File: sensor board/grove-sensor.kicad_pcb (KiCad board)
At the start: 2 copper layers, 71.8 x 71.8 mm, 27 parts, among them P1 CONN_01X03, P2 CONN_01X03, P3 CONN_01X03, P4 CONN_01X04, Q1 PN2222A, U2 SI1143, U3 Teensy_3.1

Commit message: bunch of sensor stuff
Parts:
- added P10: CONN_01X01, Pin_Headers:Pin_Header_Straight_1x01, F.Cu at (174.0, 94.0)
- added P11: CONN_01X01, Pin_Headers:Pin_Header_Straight_1x01, F.Cu at (173.5, 97.8)
- added P12: CONN_01X01, Pin_Headers:Pin_Header_Straight_1x01, F.Cu at (172.3, 101.6)
- added P13: CONN_01X01, Pin_Headers:Pin_Header_Straight_1x01, F.Cu at (170.6, 105.4)
- added P5: CONN_01X01, Pin_Headers:Pin_Header_Straight_1x01, F.Cu at (123.7, 87.8)
- added P6: CONN_01X01, Pin_Headers:Pin_Header_Straight_1x01, F.Cu at (123.2, 91.4)
- added P7: CONN_01X01, Pin_Headers:Pin_Header_Straight_1x01, F.Cu at (171.8, 82.5)
- added P8: CONN_01X01, Pin_Headers:Pin_Header_Straight_1x01, F.Cu at (173.2, 86.4)
- added P9: CONN_01X01, Pin_Headers:Pin_Header_Straight_1x01, F.Cu at (173.9, 90.2)
- added U1: ADD8704, SI1143:TSSOP-14, F.Cu at (163.8, 104.1)
- D1, D2, D3: footprint LEDs:LED-5MM -> LEDs:LED_0805
- P1, P2, P3: value CONN_01X03 -> CONN_01X01; footprint Pin_Headers:Pin_Header_Straight_1x03 -> Pin_Headers:Pin_Header_Straight_1x01
- P4: value CONN_01X04 -> CONN_01X01; footprint Pin_Headers:Pin_Header_Straight_1x04 -> Pin_Headers:Pin_Header_Straight_1x01
- Q1: footprint TO_SOT_Packages_THT:TO-92_Horizontal1_Inline_Narrow_Oval -> TO_SOT_Packages_SMD:SOT-23_Handsoldering
- moved R5 73.9 mm to (151.1, 102.9), turned to 90 degrees
- moved R2 67.3 mm to (144.8, 102.9), turned to 90 degrees
- moved R10 44.5 mm to (165.1, 133.3)
- moved R11 44.5 mm to (148.6, 133.3)
- moved R6 44.5 mm to (152.4, 135.9)
- moved R7 44.5 mm to (143.5, 135.9)
- moved R9 44.5 mm to (160.0, 135.9)
- moved R13 44.5 mm to (139.7, 121.9)
- moved R3 44.5 mm to (157.5, 124.5)
- moved C1 44.5 mm to (152.4, 123.2)
- moved C2 44.5 mm to (143.5, 130.8)
- moved C3 44.5 mm to (148.6, 123.2)
- moved R12 44.5 mm to (138.4, 128.3)
- moved R14 44.5 mm to (152.4, 128.9)
- moved R4 44.5 mm to (161.3, 128.3)
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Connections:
- P1 pad 1: GND -> +5V
- P2 pad 1: GND -> +5V
- P3 pad 1: GND -> /RGB2
- U3 pad 24: Net-(U3-Pad24) -> /3.3V
- U3 pad 3: Net-(P3-Pad2) -> Net-(P8-Pad1)
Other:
- board size 71.8 x 71.8 mm -> 50.8 x 50.8 mm

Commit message: Some fixes and placement changes
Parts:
- removed P2, P3, P4, P5, P6: CONN_01X01, Pin_Headers:Pin_Header_Straight_1x01
- added D4: LED_RGB, LEDs:LED_WS2812-PLCC6, F.Cu at (162.6, 84.3)
- added D5: LED_RGB, LEDs:LED_WS2812-PLCC6, F.Cu at (132.1, 84.6)
- added R15: 100, Resistors_SMD:R_0603_HandSoldering, F.Cu at (155.2, 86.4)
- added R16: 100, Resistors_SMD:R_0603_HandSoldering, F.Cu at (155.2, 84.3)
- added R17: 100, Resistors_SMD:R_0603_HandSoldering, F.Cu at (155.2, 82.3)
- added R18: 100, Resistors_SMD:R_0603_HandSoldering, F.Cu at (139.3, 82.4)
- added R19: 100, Resistors_SMD:R_0603_HandSoldering, F.Cu at (139.3, 84.5)
- added R20: 100, Resistors_SMD:R_0603_HandSoldering, F.Cu at (139.3, 86.5)
- moved R9 53.6 mm to (125.0, 95.4), turned to 270 degrees
- moved R10 50.8 mm to (126.4, 100.5), turned to 270 degrees
- moved R11 48.5 mm to (125.1, 90.9), turned to 90 degrees
- moved P1 45.3 mm to (169.9, 79.0)
- moved C2 41.8 mm to (128.4, 91.8)
- moved R8 40.2 mm to (135.0, 100.6), turned to 90 degrees
- moved R7 40.1 mm to (139.1, 96.0), turned to 270 degrees
- moved R6 37.5 mm to (139.1, 100.8), turned to 90 degrees
- moved R4 34.3 mm to (134.7, 106.6), turned to 180 degrees
- moved U1 32.7 mm to (132.2, 95.9), turned to 90 degrees
- moved C1 31.1 mm to (137.3, 96.0), turned to 270 degrees
- moved C3 29.1 mm to (153.9, 94.6), turned to 180 degrees
- moved R12 28.4 mm to (129.0, 101.5), turned to 90 degrees
- moved R3 28.4 mm to (137.5, 104.3), turned to 180 degrees
- moved R13 18.4 mm to (130.2, 106.2), turned to 180 degrees
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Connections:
- net /PROX_INT renamed Net-(U2-Pad4)
- C2 pad 1: /OUT -> Net-(C2-Pad1)
- P1 pad 1: +5V -> /PIR_IN
- R12 pad 1: Net-(R12-Pad1) -> Net-(C2-Pad1)
- R13 pad 2: /OUT -> Net-(C2-Pad1)
- R7 pad 2: Net-(R7-Pad2) -> Net-(R5-Pad1)
- U1 pad 8: Net-(R12-Pad1) -> Net-(C2-Pad1)
- U3 pad 20: Net-(U3-Pad20) -> /PIR_IN
- U3 pad 4: Net-(U3-Pad4) -> /LED1_R
- U3 pad 5: Net-(U3-Pad5) -> /LED1_G
- U3 pad 6: Net-(U3-Pad6) -> /LED1_B
- U3 pad 7: Net-(U3-Pad7) -> /LED2_R
- U3 pad 8: Net-(U3-Pad8) -> /LED2_G
- U3 pad 9: Net-(U3-Pad9) -> /LED2_B
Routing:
- net GND: track 0.00 -> 11.3 mm, vias 0 -> 5
- net Net-(C2-Pad2): track 0.00 -> 11.0 mm
- net Net-(R11-Pad1): track 0.00 -> 9.42 mm, vias 0 -> 2
- net /SENSITIVITY: track 0.00 -> 7.81 mm
- net Net-(C2-Pad1): track 0.00 -> 3.97 mm
- net Net-(D5-Pad6): track 0.00 -> 3.87 mm
- net Net-(D5-Pad4): track 0.00 -> 3.77 mm
- net Net-(D5-Pad5): track 0.00 -> 3.69 mm
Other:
- outline, holes or cut-outs redrawn
- copper layers 2 -> 4

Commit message: Draft sensor route on 4 layers
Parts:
- moved U3 31.8 mm to (162.6, 76.2), turned to 180 degrees
- moved D5 31.2 mm to (163.3, 84.2), turned to 180 degrees
- moved D4 28.3 mm to (134.2, 84.1), turned to 0 degrees
- moved D2 25.0 mm to (159.6, 97.0)
- moved D1 20.4 mm to (138.9, 112.3)
- moved D3 20.1 mm to (158.1, 112.3), turned to 270 degrees
- moved R14 18.4 mm to (163.8, 98.0), turned to 180 degrees
- moved U2 18.2 mm to (148.3, 96.1), turned to 90 degrees
- moved R20 17.3 mm to (156.1, 82.3), turned to 0 degrees
- moved R18 17.2 mm to (156.1, 86.4), turned to 0 degrees
- moved C3 16.8 mm to (162.2, 109.2), turned to 90 degrees
- moved R19 16.8 mm to (156.1, 84.3), turned to 0 degrees
- moved R1 15.5 mm to (142.7, 98.4)
- moved R15 14.3 mm to (141.6, 82.0), turned to 180 degrees
- moved R17 14.1 mm to (141.6, 86.1), turned to 180 degrees
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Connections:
- U3 pad 4: /LED1_R -> /LED1_B
- U3 pad 6: /LED1_B -> /LED1_R
- U3 pad 7: /LED2_R -> /LED2_B
- U3 pad 9: /LED2_B -> /LED2_R
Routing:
- net /MISO: track 0.00 -> 55.1 mm
- net /MOSI: track 0.00 -> 51.4 mm
- net Net-(C3-Pad2): track 0.00 -> 44.3 mm
- net /V_RAW: track 0.00 -> 37.1 mm
- net /PIR_IN: track 0.00 -> 34.1 mm, vias 0 -> 2
- net Net-(R5-Pad1): track 0.00 -> 32.4 mm, vias 0 -> 3
- net /3.3V: track 0.00 -> 25.6 mm, vias 0 -> 1
- net Net-(P8-Pad1): track 0.00 -> 25.0 mm
- net Net-(R1-Pad2): track 0.00 -> 24.9 mm, vias 0 -> 2
- net Net-(D3-Pad1): track 0.00 -> 24.0 mm
- net Net-(D1-Pad1): track 0.00 -> 23.1 mm, vias 0 -> 2
- net Net-(C2-Pad1): track 3.97 -> 25.0 mm, vias 0 -> 2
- net Net-(C2-Pad2): track 11.0 -> 30.2 mm, vias 0 -> 2
- net /LED1_R: track 0.00 -> 17.3 mm
- net +5V: track 0.00 -> 13.4 mm, vias 0 -> 7
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- added copper zone on Power, net +5V
- added copper zone on Ground, net GND
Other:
- outline, holes or cut-outs redrawn
- net class Default: clearance 0.2 -> 0.127; trace_width 0.25 -> 0.127; via_dia 0.6 -> 0.4572; via_drill 0.4 -> 0.254
- rule trace_clearance: 0.2 -> 0.127
- rule trace_min: 0.2 -> 0.127
- rule via_min_drill: 0.3 -> 0.254
- rule via_min_size: 0.4 -> 0.4572

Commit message: Fixes and updates to sensor board
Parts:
- removed D4, D5: LED_RGB, LEDs:LED_WS2812-PLCC6
- removed P10, P11, P12, P13: CONN_01X01, Pin_Headers:Pin_Header_Straight_1x01
- removed R15, R16, R17, R18, R19, R20: 100, Resistors_SMD:R_0603_HandSoldering
- added C4: 10uF, Capacitors_SMD:C_0603_HandSoldering, F.Cu at (143.5, 69.6)
- added C5: 0.1uF, Capacitors_SMD:C_0603_HandSoldering, F.Cu at (138.0, 88.9)
- added C6: 0.1uF, Capacitors_SMD:C_0603_HandSoldering, F.Cu at (161.4, 78.7)
- added P2: CONN_01X06, Pin_Headers:Pin_Header_Straight_1x06, F.Cu at (155.1, 72.0)
- added P3: CONN_01X01, Pin_Headers:Pin_Header_Straight_1x01, F.Cu at (171.6, 98.6)
- added P4: CONN_01X01, Pin_Headers:Pin_Header_Straight_1x01, F.Cu at (171.6, 93.0)
- added R21: 0, Resistors_SMD:R_0603_HandSoldering, F.Cu at (142.9, 95.0)
- added R22: 0, Resistors_SMD:R_0603_HandSoldering, F.Cu at (144.7, 95.0)
- added R23: 10k, Resistors_SMD:R_0603_HandSoldering, F.Cu at (154.4, 98.3)
- added R24: 10k, Resistors_SMD:R_0603_HandSoldering, F.Cu at (154.4, 96.9)
- added R25: 0, Resistors_SMD:R_0603_HandSoldering, F.Cu at (132.5, 83.7)
- added R26: 10k, Resistors_SMD:R_0603_HandSoldering, F.Cu at (167.1, 87.8)
- added U4: MCP1700, TO_SOT_Packages_SMD:SOT-23, F.Cu at (166.5, 94.9)
- added U5: WS2812B, LEDs:LED_WS2812B-PLCC4, F.Cu at (138.7, 84.1)
- added U6: WS2812B, LEDs:LED_WS2812B-PLCC4, F.Cu at (161.0, 83.8)
- Q1: value PN2222A -> Q_NPN_BEC; footprint TO_SOT_Packages_SMD:SOT-23_Handsoldering -> TO_SOT_Packages_SMD:SOT-23
- R2: footprint Resistors_SMD:R_0402 -> Resistors_SMD:R_0603
- moved P1 16.8 mm to (171.6, 95.8)
- moved Q1 1.08 mm to (132.7, 102.9), turned to 180 degrees
- moved R1 0.51 mm to (142.7, 98.9)
- moved P9 0.13 mm to (173.7, 89.7)
- moved R5 0.09 mm to (151.5, 106.6)
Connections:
- net /CS renamed Net-(U3-Pad10)
- Q1 pad 1: /V_RAW -> Net-(Q1-Pad1)
- Q1 pad 2: Net-(Q1-Pad2) -> /V_RAW
- R8 pad 1: Net-(Q1-Pad2) -> Net-(Q1-Pad1)
- U2 pad 1: /SDA -> Net-(R21-Pad1)
- U2 pad 2: /SCL -> Net-(R22-Pad1)
- U3 pad 1: /RGB1 -> Net-(P2-Pad2)
- U3 pad 11: /MOSI -> Net-(U3-Pad11)
- U3 pad 12: /MISO -> Net-(U3-Pad12)
- U3 pad 2: /RGB2 -> Net-(P2-Pad4)
- U3 pad 4: /LED1_B -> Net-(U3-Pad4)
- U3 pad 5: /LED1_G -> Net-(U3-Pad5)
- U3 pad 6: /LED1_R -> Net-(U3-Pad6)
- U3 pad 7: /LED2_B -> Net-(U3-Pad7)
- U3 pad 8: /LED2_G -> /LED_IN
- U3 pad 9: /LED2_R -> Net-(U3-Pad9)
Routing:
- net /MISO: track 55.1 -> 0.00 mm
- net /MOSI: track 51.4 -> 0.00 mm
- net Net-(P2-Pad4): track 0.00 -> 42.8 mm
- net +5V: track 13.4 -> 38.6 mm, vias 7 -> 10
- net Net-(U5-Pad2): track 0.00 -> 23.5 mm
- net /LED1_R: track 17.3 -> 0.00 mm
- net Net-(P2-Pad3): track 0.00 -> 16.3 mm
- net Net-(P2-Pad2): track 0.00 -> 13.6 mm
- net Net-(R21-Pad1): track 0.00 -> 13.3 mm
- net Net-(R22-Pad1): track 0.00 -> 13.1 mm, vias 0 -> 3
- net /3.3V: track 25.6 -> 38.5 mm, vias 1 -> 2
- net /LED1_G: track 12.5 -> 0.00 mm
- net /LED2_B: track 11.7 -> 0.00 mm
- net /LED2_G: track 9.95 -> 0.00 mm
- net /LED_IN: track 0.00 -> 9.15 mm
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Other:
- net class Default: trace_width 0.127 -> 0.254

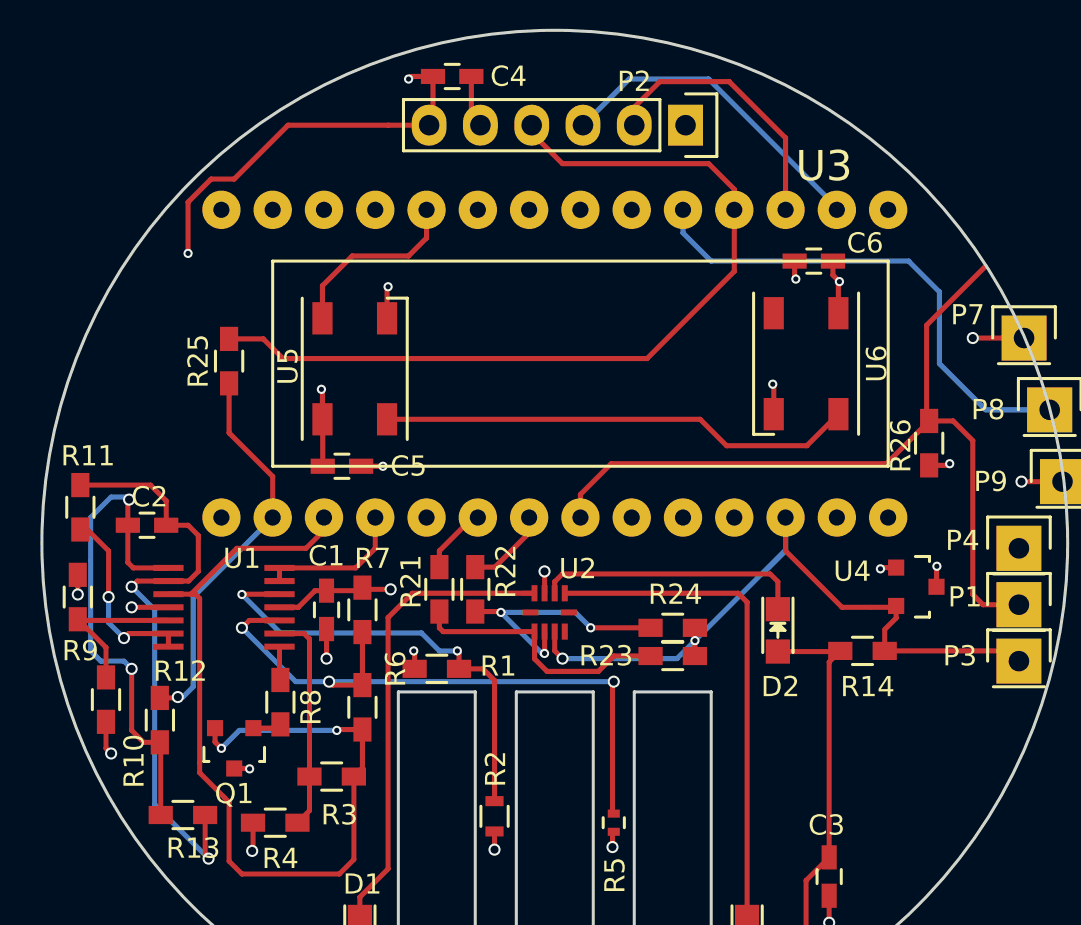
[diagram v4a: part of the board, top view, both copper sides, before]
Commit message: Added sensor mounting holes
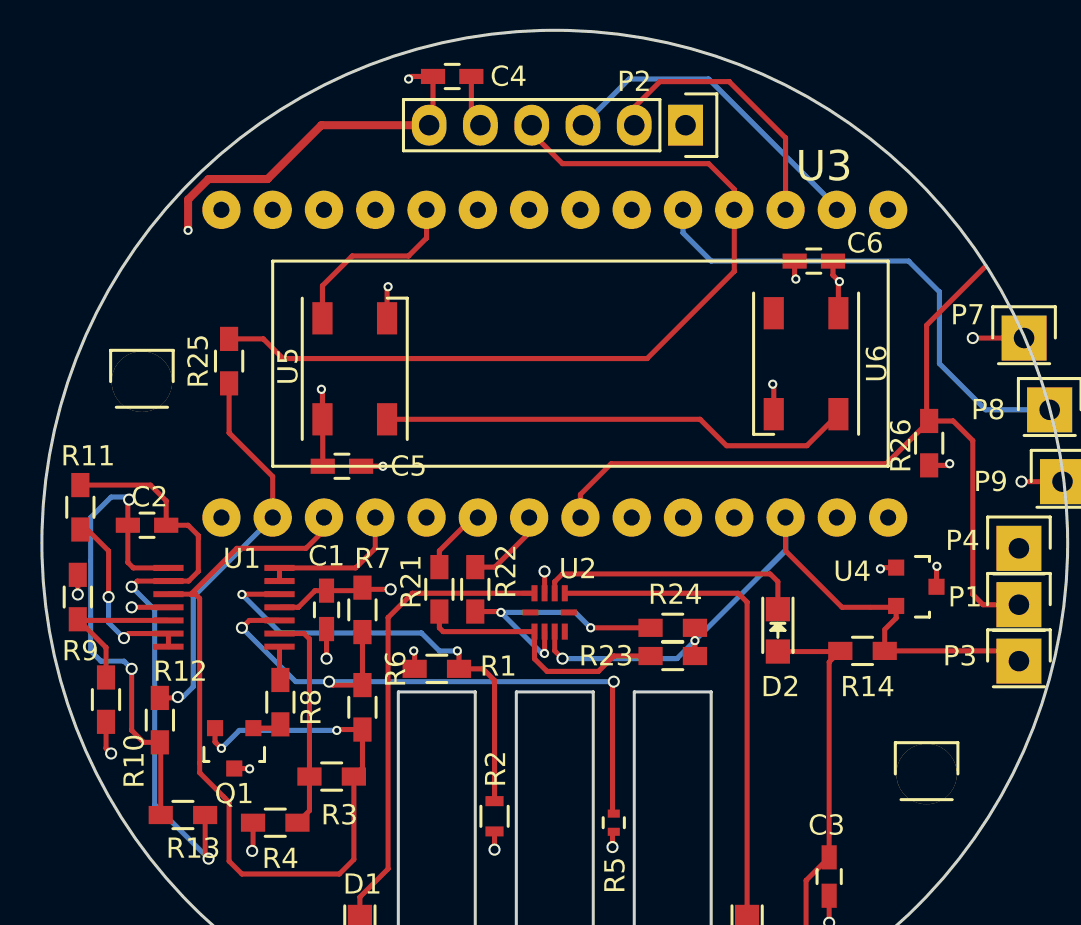
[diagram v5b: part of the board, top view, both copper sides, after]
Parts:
- added P5: CONN_01X01, Pin_Headers:Pin_Header_Straight_1x01, F.Cu at (167.0, 104.1)
- added P6: CONN_01X01, Pin_Headers:Pin_Header_Straight_1x01, F.Cu at (128.1, 84.7)
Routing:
- net +5V: track 38.6 -> 37.5 mm
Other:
- net class Default: trace_width 0.254 -> 0.4
- net class Power added: clearance 0.127, trace_width 0.254, via_dia 0.4572, via_drill 0.254
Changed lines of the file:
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@@
     (thickness 1.6)
     (drawings 13)
-    (tracks 340)
+    (tracks 339)
     (zones 0)
-    (modules 43)
-    (nets 48)
+    (modules 45)
+    (nets 50)
   )
   (page A4)
@@
   )
   (setup
-    (last_trace_width 0.254)
+    (last_trace_width 0.4)
     (trace_clearance 0.127)
     (zone_clearance 0.508)
@@
     (mod_text_size 1 1)
     (mod_text_width 0.15)
-    (pad_size 1.524 1.524)
-    (pad_drill 0.762)
+    (pad_size 3 3)
+    (pad_drill 3)
     (pad_to_mask_clearance 0.2)
     (aux_axis_origin 0 0)
@@
   (net 46 "Net-(U6-Pad2)")
   (net 47 "Net-(Q1-Pad1)")
+  (net 48 "Net-(P5-Pad1)")
+  (net 49 "Net-(P6-Pad1)")
   (net_class Default "This is the default net class."
     (clearance 0.127)
-    (trace_width 0.254)
+    (trace_width 0.4)
     (via_dia 0.4572)
     (via_drill 0.254)
@@
     (add_net "Net-(P2-Pad3)")
     (add_net "Net-(P2-Pad4)")
+    (add_net "Net-(P5-Pad1)")
+    (add_net "Net-(P6-Pad1)")
     (add_net "Net-(P8-Pad1)")
     (add_net "Net-(Q1-Pad1)")
@@
     (add_net "Net-(U5-Pad2)")
     (add_net "Net-(U6-Pad2)")
+  )
+  (net_class Power ""
+    (clearance 0.127)
+    (trace_width 0.254)
+    (via_dia 0.4572)
+    (via_drill 0.254)
+    (uvia_dia 0.762)
+    (uvia_drill 0.508)
   )
   (module Teensy-3:Teensy-3.1 (layer Top)
@@
     )
   )
+  (module Pin_Headers:Pin_Header_Straight_1x01 (layer Top)
+    (at 128.143 84.709)
+    (descr "Through hole pin header")
+    (tags "pin header")
+    (fp_text reference P6 (at -14.732 -4.699) (layer F.SilkS) hide
+      (effects (font (size 1 1) (thickness 0.15)))
+    )
+    (fp_text value CONN_01X01 (at -12.954 -2.032) (layer F.Fab) hide
+      (effects (font (size 1 1) (thickness 0.15)))
+    )
+    (fp_line (start 1.55 -1.55) (end 1.55 0) (layer F.SilkS) (width 0.15))
+    (fp_line (start -1.75 -1.75) (end -1.75 1.75) (layer F.CrtYd) (width 0.05))
+    (fp_line (start 1.75 -1.75) (end 1.75 1.75) (layer F.CrtYd) (width 0.05))
+    (fp_line (start -1.75 -1.75) (end 1.75 -1.75) (layer F.CrtYd) (width 0.05))
+    (fp_line (start -1.75 1.75) (end 1.75 1.75) (layer F.CrtYd) (width 0.05))
+    (fp_line (start -1.55 0) (end -1.55 -1.55) (layer F.SilkS) (width 0.15))
+    (fp_line (start -1.55 -1.55) (end 1.55 -1.55) (layer F.SilkS) (width 0.15))
+    (fp_line (start -1.27 1.27) (end 1.27 1.27) (layer F.SilkS) (width 0.15))
+    (pad 1 thru_hole circle (at 0 0) (size 3 3) (drill 3) (layers *.Cu *.Mask F.SilkS)
+      (net 49 "Net-(P6-Pad1)"))
+    (model Pin_Headers.3dshapes/Pin_Header_Straight_1x01.wrl
+      (at (xyz 0 0 0))
+      (scale (xyz 1 1 1))
+      (rotate (xyz 0 0 90))
+    )
+  )
+  (module Pin_Headers:Pin_Header_Straight_1x01 (layer Top)
+    (at 167.005 104.14)
+    (descr "Through hole pin header")
+    (tags "pin header")
+    (fp_text reference P5 (at -53.467 -15.621) (layer F.SilkS) hide
+      (effects (font (size 1 1) (thickness 0.15)))
+    )
+    (fp_text value CONN_01X01 (at -53.848 -18.542) (layer F.Fab) hide
+      (effects (font (size 1 1) (thickness 0.15)))
+    )
+    (fp_line (start 1.55 -1.55) (end 1.55 0) (layer F.SilkS) (width 0.15))
+    (fp_line (start -1.75 -1.75) (end -1.75 1.75) (layer F.CrtYd) (width 0.05))
+    (fp_line (start 1.75 -1.75) (end 1.75 1.75) (layer F.CrtYd) (width 0.05))
+    (fp_line (start -1.75 -1.75) (end 1.75 -1.75) (layer F.CrtYd) (width 0.05))
+    (fp_line (start -1.75 1.75) (end 1.75 1.75) (layer F.CrtYd) (width 0.05))
+    (fp_line (start -1.55 0) (end -1.55 -1.55) (layer F.SilkS) (width 0.15))
+    (fp_line (start -1.55 -1.55) (end 1.55 -1.55) (layer F.SilkS) (width 0.15))
+    (fp_line (start -1.27 1.27) (end 1.27 1.27) (layer F.SilkS) (width 0.15))
+    (pad 1 thru_hole circle (at 0 0) (size 3 3) (drill 3) (layers *.Cu *.Mask F.SilkS)
+      (net 48 "Net-(P5-Pad1)"))
+    (model Pin_Headers.3dshapes/Pin_Header_Straight_1x01.wrl
+      (at (xyz 0 0 0))
+      (scale (xyz 1 1 1))
+      (rotate (xyz 0 0 90))
+    )
+  )
   (gr_line (start 144.653 115.316) (end 144.653 100.076) (angle 90) (layer Edge.Cuts) (width 0.15))
   (gr_line (start 140.843 115.316) (end 144.653 115.316) (angle 90) (layer Edge.Cuts) (width 0.15))
@@
   (gr_line (start 146.685 100.076) (end 146.685 115.316) (angle 90) (layer Edge.Cuts) (width 0.15))
   (gr_circle (center 148.59 92.71) (end 173.99 92.71) (layer Edge.Cuts) (width 0.15))
+  (segment (start 142.367 72.009) (end 137.033 72.009) (width 0.4) (layer Top) (net 1))
+  (via (at 130.429 77.216) (size 0.4572) (drill 0.254) (layers Top Bottom) (net 1))
+  (segment (start 130.429 75.692) (end 130.429 77.216) (width 0.4) (layer Top) (net 1))
+  (segment (start 131.445 74.676) (end 130.429 75.692) (width 0.4) (layer Top) (net 1))
+  (segment (start 134.366 74.676) (end 131.445 74.676) (width 0.4) (layer Top) (net 1))
+  (segment (start 137.033 72.009) (end 134.366 74.676) (width 0.4) (layer Top) (net 1))
   (segment (start 132.715 103.86822) (end 133.45922 103.86822) (width 0.254) (layer Top) (net 1))
   (via (at 133.477 103.886) (size 0.4572) (drill 0.254) (layers Top Bottom) (net 1))
@@
   (via (at 167.513 93.853) (size 0.4572) (drill 0.254) (layers Top Bottom) (net 1))
   (segment (start 167.49522 93.87078) (end 167.513 93.853) (width 0.254) (layer Top) (net 1))
-  (segment (start 140.335 72.009) (end 135.382 72.009) (width 0.254) (layer Top) (net 1))
-  (segment (start 135.382 72.009) (end 132.715 74.676) (width 0.254) (layer Top) (net 1))
-  (segment (start 132.715 74.676) (end 131.572 74.676) (width 0.254) (layer Top) (net 1))
-  (segment (start 131.572 74.676) (end 130.429 75.819) (width 0.254) (layer Top) (net 1))
-  (segment (start 130.429 75.819) (end 130.429 78.359) (width 0.254) (layer Top) (net 1))
-  (via (at 130.429 78.359) (size 0.4572) (drill 0.254) (layers Top Bottom) (net 1))
-  (segment (start 142.367 72.009) (end 140.335 72.009) (width 0.254) (layer Top) (net 1))
   (segment (start 141.648 98.933) (end 141.648 98.087) (width 0.254) (layer Top) (net 1))
   (via (at 141.605 98.044) (size 0.4572) (drill 0.254) (layers Top Bottom) (net 1))
